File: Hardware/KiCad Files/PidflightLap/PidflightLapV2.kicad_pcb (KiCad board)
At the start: 2 copper layers, 150 x 150 mm, 32 parts, among them SW1 SW_SPST, U1 HC_06, U2 RX5808, U3 Arduino_Nano_v3.x, U4 RX5808, U5 Arduino_Nano_v3.x, U6 RX5808, U7 Arduino_Nano_v3.x, U8 RX5808, U9 Arduino_Nano_v3.x

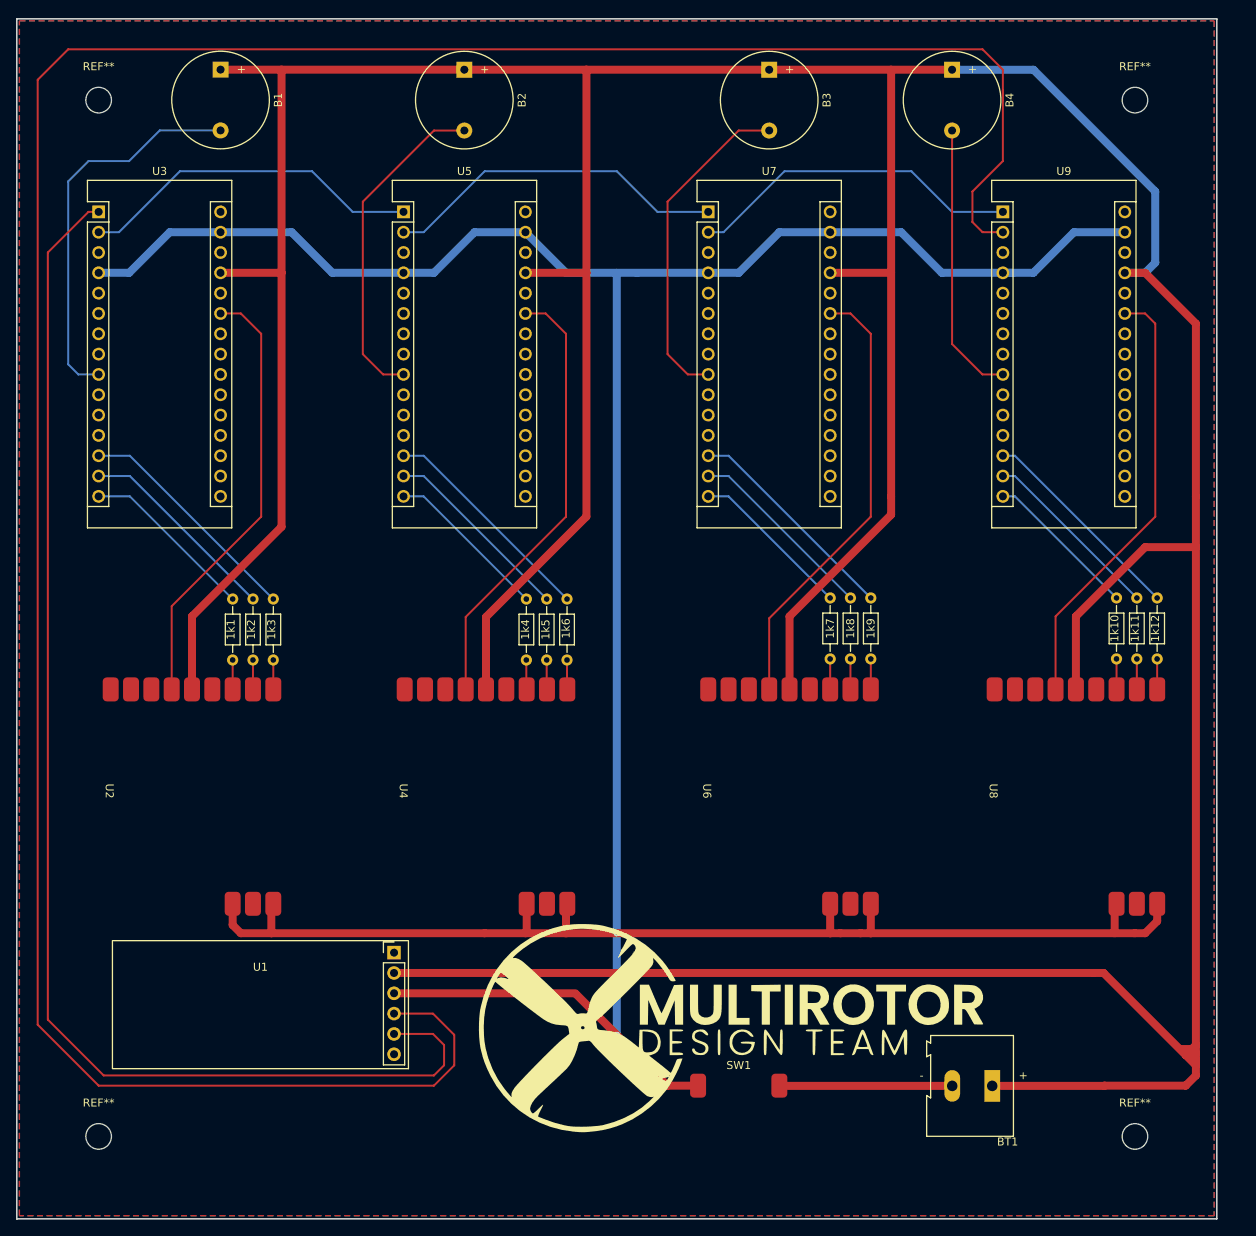
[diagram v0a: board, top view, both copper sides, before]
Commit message: Cleaned Up Files and added Bevels and BOM
removed some pointless KiCAD files I had accidently added created as well as beveled all the 90 degree connections on the PCB file
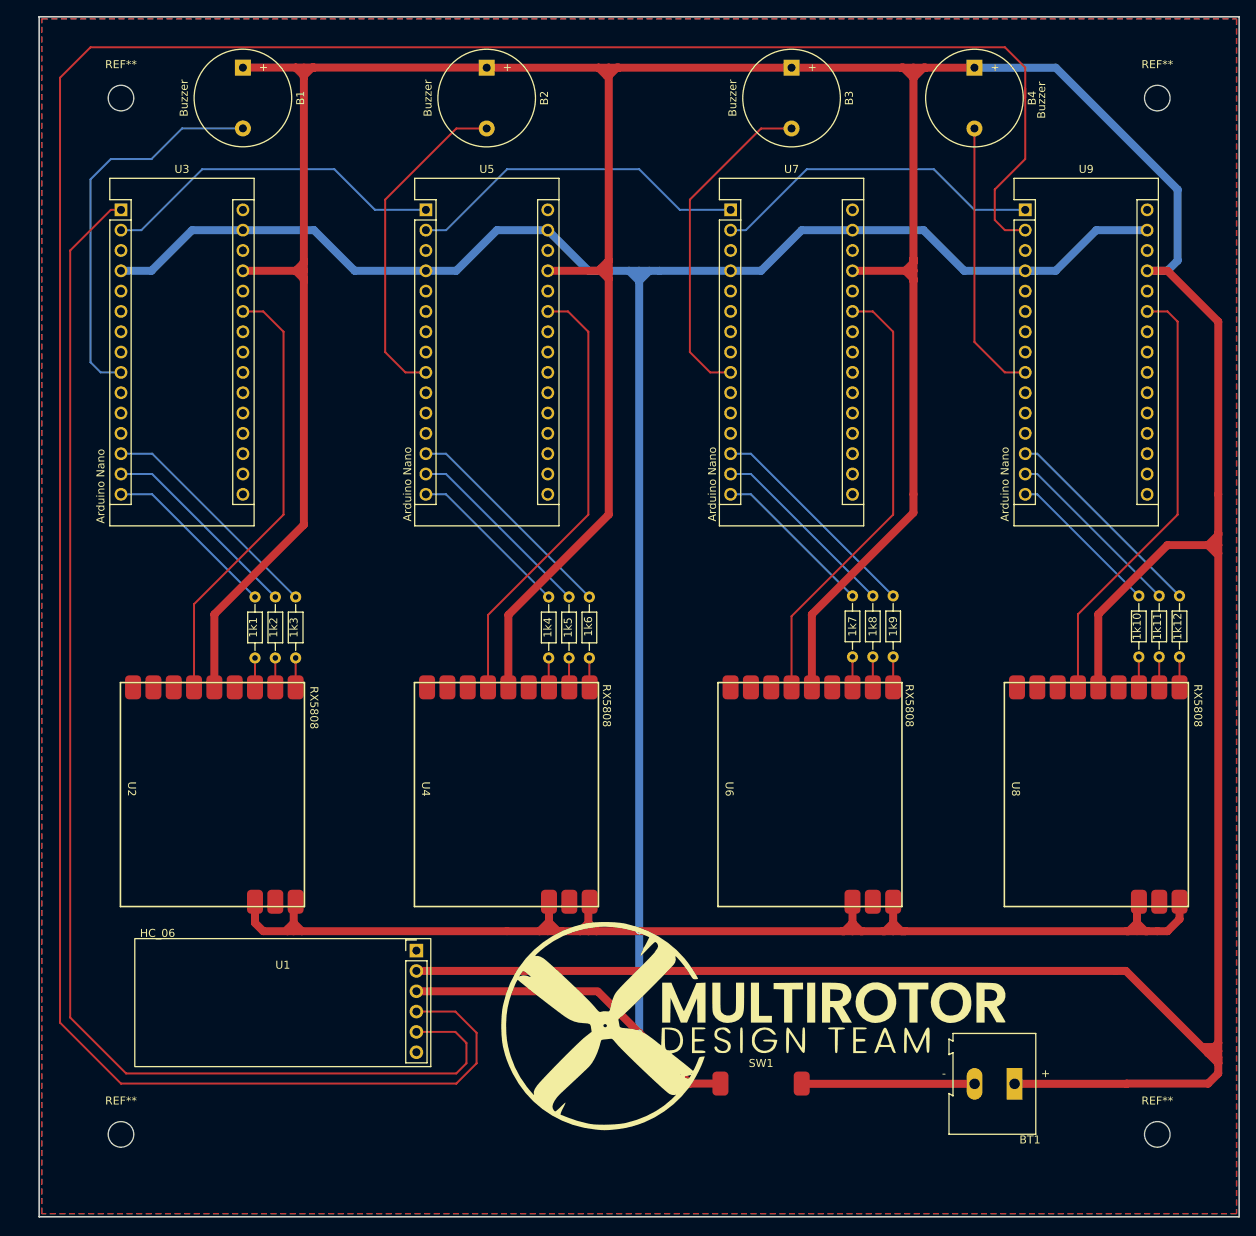
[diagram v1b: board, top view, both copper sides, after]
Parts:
- moved 1k4 2.81 mm to (82.9, 92.6)
- moved 1k6 2.81 mm to (88.0, 92.6)
- moved B3 2.81 mm to (113.3, 26.4)
- moved B4 2.81 mm to (136.1, 26.4)
- moved U4 2.81 mm to (72.6, 116.6)
- moved U9 2.81 mm to (142.5, 44.2)
- moved 1k10 2.81 mm to (156.7, 92.5)
- moved 1k11 2.81 mm to (159.2, 92.5)
- moved 1k1 2.81 mm to (46.2, 92.6)
- moved 1k2 2.81 mm to (48.8, 92.6)
- moved B1 2.81 mm to (44.7, 26.4)
- moved REF** 2.81 mm to (29.5, 159.8)
- moved U1 2.81 mm to (68.2, 151.3)
- moved 1k3 2.81 mm to (51.3, 92.6)
- moved 1k5 2.81 mm to (85.5, 92.6)
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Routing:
- net +5V: track 676.6 -> 701.3 mm
- net GND: track 426.0 -> 449.4 mm
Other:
- board text added: "10.1mm"
- board text added: "14.348mm"
- board text added: "Arduino Nano"
- board text added: "Buzzer"
- board text added: "HC_06"
- board text added: "RX5808"

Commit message: Added Gerber Files
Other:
- board text added: "C. Buneta"
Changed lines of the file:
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@@
   (gr_line (start 29.544 30.066) (end 29.544 20.066) (layer "Dwgs.User") (width 0.15))
   (gr_rect (start 19.234 20.066) (end 169.234 170.066) (layer "Edge.Cuts") (width 0.2) (fill none))
+  (gr_text "C. Buneta" (at 39.878 167.894) (layer "F.SilkS")
+    (effects (font (size 1 1) (thickness 0.15)))
+  )
   (gr_text "RX5808" (at 164.084 106.172 270) (layer "F.SilkS")
     (effects (font (size 1 1) (thickness 0.15)))
